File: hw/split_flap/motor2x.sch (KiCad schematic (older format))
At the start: 4 parts, among them J10 Conn_01x05, J9 Conn_01x05, U3 PCF8574, U4 ULN2803A

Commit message: hw: Supercharge PCB !
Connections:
- net L2: now reaches U4.6 (I6)
- net L2: now also U3.5 (P1); no longer U3.10 (P5)
- net L3: now reaches U4.7 (I7)
- net L3: now also U3.6 (P2); no longer U3.11 (P6)
- net L4: now reaches U4.8 (I8)
- net L4: now also U3.7 (P3); no longer U3.12 (P7)
- net L1: now reaches U3.4 (P0)
- net L1: now also U4.5 (I5); no longer U4.4 (I4)
- net L7: now reaches U4.3 (I3)
- net L7: now also U3.11 (P6); no longer U3.5 (P1)
- net L6: now reaches U4.2 (I2)
- net L6: now also U3.10 (P5); no longer U3.6 (P2)
- net L5: now reaches U4.1 (I1)
- net L5: now also U3.9 (P4); no longer U3.7 (P3)
- new net L8: U3.12 (P7), U4.4 (I4)
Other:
- moved on the sheet: J21, J22, U13, U14

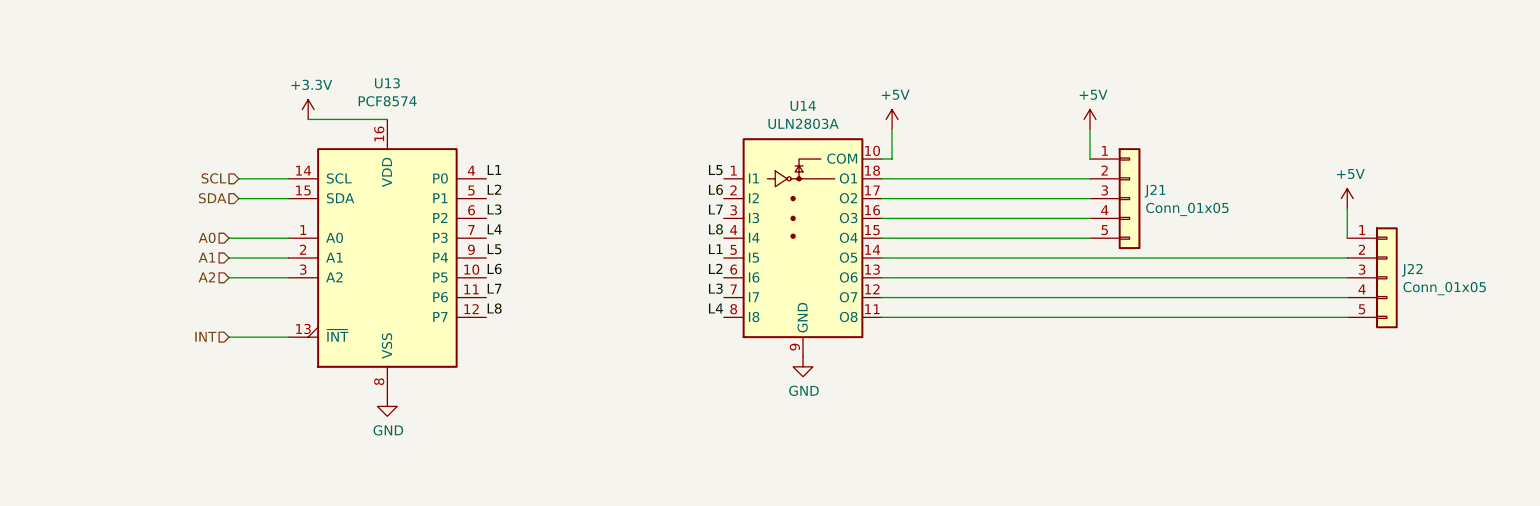
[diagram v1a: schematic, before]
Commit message: Reroute full PCB
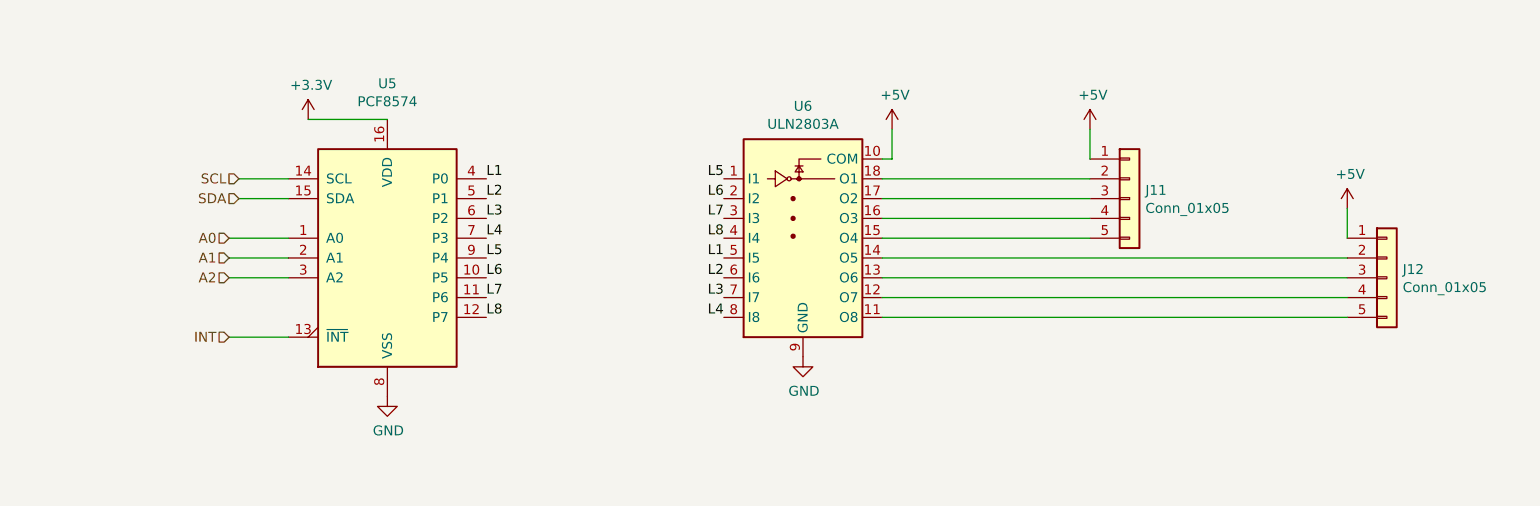
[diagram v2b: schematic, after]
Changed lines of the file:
@@
 AR Path="/5DEBFEF8/5E0DED8E" Ref="#PWR0150"  Part="1"
 AR Path="/5DED9C19/5E0DED8E" Ref="#PWR0156"  Part="1"
-F 0 "#PWR0156" H 9350 3000 50  0001 C CNN
+F 0 "#PWR0128" H 9350 3000 50  0001 C CNN
 F 1 "+5V" H 9365 3323 50  0000 C CNN
 F 2 "" H 9350 3150 50  0001 C CNN
@@
 AR Path="/5DEBFEF8/5E0DED94" Ref="J20"  Part="1"
 AR Path="/5DED9C19/5E0DED94" Ref="J22"  Part="1"
-F 0 "J22" H 9630 3542 50  0000 L CNN
+F 0 "J12" H 9630 3542 50  0000 L CNN
 F 1 "Conn_01x05" H 9630 3451 50  0000 L CNN
 F 2 "Connector_JST:JST_XH_B5B-XH-A_1x05_P2.50mm_Vertical" H 9550 3500 50  0001 C CNN
@@
 AR Path="/5DEBFEF8/5E0DED9D" Ref="#PWR0151"  Part="1"
 AR Path="/5DED9C19/5E0DED9D" Ref="#PWR0157"  Part="1"
-F 0 "#PWR0157" H 8050 2600 50  0001 C CNN
+F 0 "#PWR0129" H 8050 2600 50  0001 C CNN
 F 1 "+5V" H 8065 2923 50  0000 C CNN
 F 2 "" H 8050 2750 50  0001 C CNN
@@
 AR Path="/5DEBFEF8/5E0DEDA9" Ref="#PWR0152"  Part="1"
 AR Path="/5DED9C19/5E0DEDA9" Ref="#PWR0158"  Part="1"
-F 0 "#PWR0158" H 7050 2600 50  0001 C CNN
+F 0 "#PWR0131" H 7050 2600 50  0001 C CNN
 F 1 "+5V" H 7065 2923 50  0000 C CNN
 F 2 "" H 7050 2750 50  0001 C CNN
@@
 AR Path="/5DEBFEF8/5E0DEDAF" Ref="#PWR0153"  Part="1"
 AR Path="/5DED9C19/5E0DEDAF" Ref="#PWR0159"  Part="1"
-F 0 "#PWR0159" H 4500 3850 50  0001 C CNN
+F 0 "#PWR0132" H 4500 3850 50  0001 C CNN
 F 1 "GND" H 4505 3927 50  0000 C CNN
 F 2 "" H 4500 4100 50  0001 C CNN
@@
 AR Path="/5DEBFEF8/5E0DEDB5" Ref="#PWR0154"  Part="1"
 AR Path="/5DED9C19/5E0DEDB5" Ref="#PWR0160"  Part="1"
-F 0 "#PWR0160" H 6600 3650 50  0001 C CNN
+F 0 "#PWR0133" H 6600 3650 50  0001 C CNN
 F 1 "GND" H 6605 3727 50  0000 C CNN
 F 2 "" H 6600 3900 50  0001 C CNN
@@
 AR Path="/5DEBFEF8/5E0DEDBB" Ref="J18"  Part="1"
 AR Path="/5DED9C19/5E0DEDBB" Ref="J21"  Part="1"
-F 0 "J21" H 8330 3142 50  0000 L CNN
+F 0 "J11" H 8330 3142 50  0000 L CNN
 F 1 "Conn_01x05" H 8330 3051 50  0000 L CNN
 F 2 "Connector_JST:JST_XH_B5B-XH-A_1x05_P2.50mm_Vertical" H 8250 3100 50  0001 C CNN
@@
 AR Path="/5DEBFEF8/5E0DEDC5" Ref="U11"  Part="1"
 AR Path="/5DED9C19/5E0DEDC5" Ref="U13"  Part="1"
-F 0 "U13" H 4500 4281 50  0000 C CNN
+F 0 "U5" H 4500 4281 50  0000 C CNN
 F 1 "PCF8574" H 4500 4190 50  0000 C CNN
 F 2 "Package_SO:SOIC-16W_7.5x10.3mm_P1.27mm" H 4500 3400 50  0001 C CNN
@@
 AR Path="/5DEBFEF8/5E0DEDCB" Ref="U12"  Part="1"
 AR Path="/5DED9C19/5E0DEDCB" Ref="U14"  Part="1"
-F 0 "U14" H 6600 3767 50  0000 C CNN
+F 0 "U6" H 6600 3767 50  0000 C CNN
 F 1 "ULN2803A" H 6600 3676 50  0000 C CNN
 F 2 "Package_SO:SOP-18_7x12.5mm_P1.27mm" H 6650 2550 50  0001 L CNN
@@
 AR Path="/5DEBFEF8/5E2206F1" Ref="#PWR0155"  Part="1"
 AR Path="/5DED9C19/5E2206F1" Ref="#PWR0161"  Part="1"
-F 0 "#PWR0161" H 4100 2550 50  0001 C CNN
+F 0 "#PWR06" H 4100 2550 50  0001 C CNN
 F 1 "+3.3V" H 4115 2873 50  0000 C CNN
 F 2 "" H 4100 2700 50  0001 C CNN

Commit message: hw: Route pcb completely
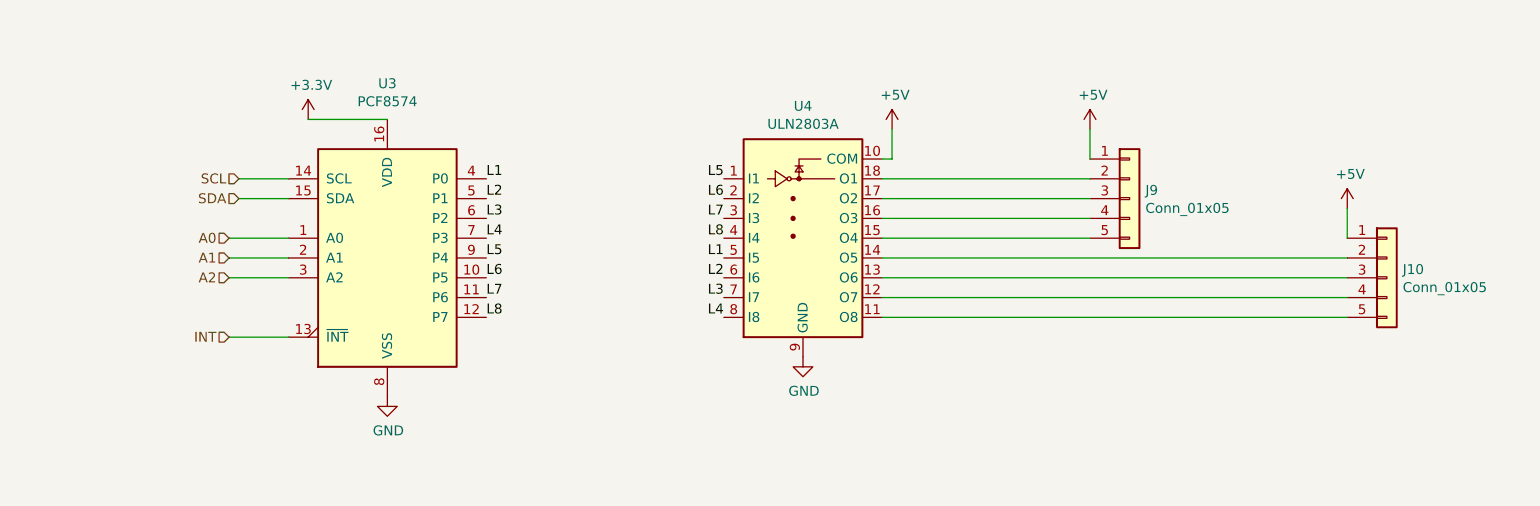
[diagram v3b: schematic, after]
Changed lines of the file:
@@
 $Descr A4 11693 8268
 encoding utf-8
-Sheet 3 7
+Sheet 2 7
 Title ""
 Date ""
@@
 AR Path="/5DEBFEF8/5E0DED8E" Ref="#PWR0150"  Part="1"
 AR Path="/5DED9C19/5E0DED8E" Ref="#PWR0156"  Part="1"
-F 0 "#PWR0128" H 9350 3000 50  0001 C CNN
+F 0 "#PWR0156" H 9350 3000 50  0001 C CNN
 F 1 "+5V" H 9365 3323 50  0000 C CNN
 F 2 "" H 9350 3150 50  0001 C CNN
@@
 AR Path="/5DEBFEF8/5E0DED94" Ref="J20"  Part="1"
 AR Path="/5DED9C19/5E0DED94" Ref="J22"  Part="1"
-F 0 "J12" H 9630 3542 50  0000 L CNN
+F 0 "J10" H 9630 3542 50  0000 L CNN
 F 1 "Conn_01x05" H 9630 3451 50  0000 L CNN
 F 2 "Connector_JST:JST_XH_B5B-XH-A_1x05_P2.50mm_Vertical" H 9550 3500 50  0001 C CNN
@@
 AR Path="/5DEBFEF8/5E0DED9D" Ref="#PWR0151"  Part="1"
 AR Path="/5DED9C19/5E0DED9D" Ref="#PWR0157"  Part="1"
-F 0 "#PWR0129" H 8050 2600 50  0001 C CNN
+F 0 "#PWR0157" H 8050 2600 50  0001 C CNN
 F 1 "+5V" H 8065 2923 50  0000 C CNN
 F 2 "" H 8050 2750 50  0001 C CNN
@@
 AR Path="/5DEBFEF8/5E0DEDA9" Ref="#PWR0152"  Part="1"
 AR Path="/5DED9C19/5E0DEDA9" Ref="#PWR0158"  Part="1"
-F 0 "#PWR0131" H 7050 2600 50  0001 C CNN
+F 0 "#PWR0158" H 7050 2600 50  0001 C CNN
 F 1 "+5V" H 7065 2923 50  0000 C CNN
 F 2 "" H 7050 2750 50  0001 C CNN
@@
 AR Path="/5DEBFEF8/5E0DEDAF" Ref="#PWR0153"  Part="1"
 AR Path="/5DED9C19/5E0DEDAF" Ref="#PWR0159"  Part="1"
-F 0 "#PWR0132" H 4500 3850 50  0001 C CNN
+F 0 "#PWR0159" H 4500 3850 50  0001 C CNN
 F 1 "GND" H 4505 3927 50  0000 C CNN
 F 2 "" H 4500 4100 50  0001 C CNN
@@
 AR Path="/5DEBFEF8/5E0DEDB5" Ref="#PWR0154"  Part="1"
 AR Path="/5DED9C19/5E0DEDB5" Ref="#PWR0160"  Part="1"
-F 0 "#PWR0133" H 6600 3650 50  0001 C CNN
+F 0 "#PWR0160" H 6600 3650 50  0001 C CNN
 F 1 "GND" H 6605 3727 50  0000 C CNN
 F 2 "" H 6600 3900 50  0001 C CNN
@@
 AR Path="/5DEBFEF8/5E0DEDBB" Ref="J18"  Part="1"
 AR Path="/5DED9C19/5E0DEDBB" Ref="J21"  Part="1"
-F 0 "J11" H 8330 3142 50  0000 L CNN
+F 0 "J9" H 8330 3142 50  0000 L CNN
 F 1 "Conn_01x05" H 8330 3051 50  0000 L CNN
 F 2 "Connector_JST:JST_XH_B5B-XH-A_1x05_P2.50mm_Vertical" H 8250 3100 50  0001 C CNN
@@
 AR Path="/5DEBFEF8/5E0DEDC5" Ref="U11"  Part="1"
 AR Path="/5DED9C19/5E0DEDC5" Ref="U13"  Part="1"
-F 0 "U5" H 4500 4281 50  0000 C CNN
+F 0 "U3" H 4500 4281 50  0000 C CNN
 F 1 "PCF8574" H 4500 4190 50  0000 C CNN
 F 2 "Package_SO:SOIC-16W_7.5x10.3mm_P1.27mm" H 4500 3400 50  0001 C CNN
@@
 AR Path="/5DEBFEF8/5E0DEDCB" Ref="U12"  Part="1"
 AR Path="/5DED9C19/5E0DEDCB" Ref="U14"  Part="1"
-F 0 "U6" H 6600 3767 50  0000 C CNN
+F 0 "U4" H 6600 3767 50  0000 C CNN
 F 1 "ULN2803A" H 6600 3676 50  0000 C CNN
 F 2 "Package_SO:SOP-18_7x12.5mm_P1.27mm" H 6650 2550 50  0001 L CNN
@@
 AR Path="/5DEBFEF8/5E2206F1" Ref="#PWR0155"  Part="1"
 AR Path="/5DED9C19/5E2206F1" Ref="#PWR0161"  Part="1"
-F 0 "#PWR06" H 4100 2550 50  0001 C CNN
+F 0 "#PWR0161" H 4100 2550 50  0001 C CNN
 F 1 "+3.3V" H 4115 2873 50  0000 C CNN
 F 2 "" H 4100 2700 50  0001 C CNN

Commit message: Update schematic with 74HC595
Remove PCF for output and use shift register
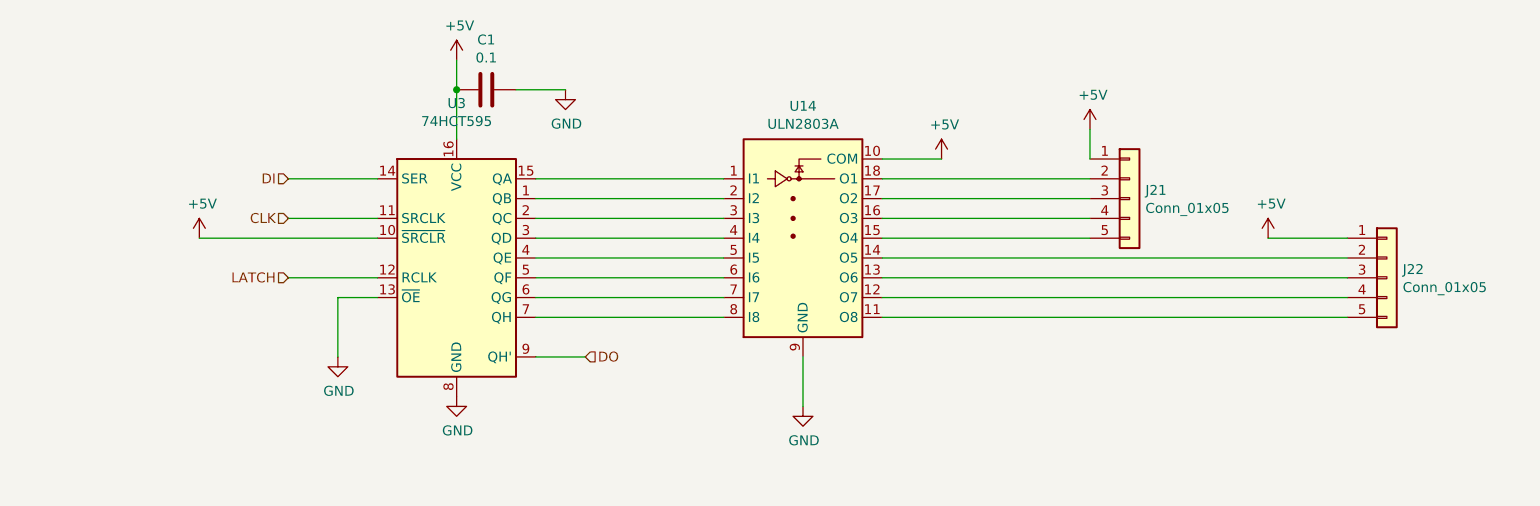
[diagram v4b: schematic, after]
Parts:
- removed U3: PCF8574, Package_SO:SOIC-16W_7.5x10.3mm_P1.27mm, symbol Interface_Expansion:PCF8574
- added C1: 0.1, symbol Device:C
- added U3: 74HCT595, symbol 74xx:74HCT595
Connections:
- net +5V: now also C1.1, U3.10 (~SRCLR), U3.16 (VCC)
- net GND: now also C1.2, U3.13 (~OE), U3.8 (GND)
- net L1: no longer names the net of U4.5 (I5)
- net L1: now also U3.4 (QE)
- net L2: no longer names the net of U4.6 (I6)
- net L2: now also U3.5 (QF)
- net L3: no longer names the net of U4.7 (I7)
- net L3: now also U3.6 (QG)
- net L4: no longer names the net of U4.8 (I8)
- net L4: now also U3.7 (QH)
- net L5: no longer names the net of U4.1 (I1)
- net L5: now also U3.15 (QA)
- net L6: no longer names the net of U4.2 (I2)
- net L6: now also U3.1 (QB)
- net L7: no longer names the net of U4.3 (I3)
- net L7: now also U3.2 (QC)
- net L8: no longer names the net of U4.4 (I4)
- net L8: now also U3.3 (QD)
- new net CLK: U3.11 (SRCLK)
- new net DI: U3.14 (SER)
- new net DO: U3.9 (QH')
- new net LATCH: U3.12 (RCLK)

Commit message: Rework PCB
Start routing all expanders
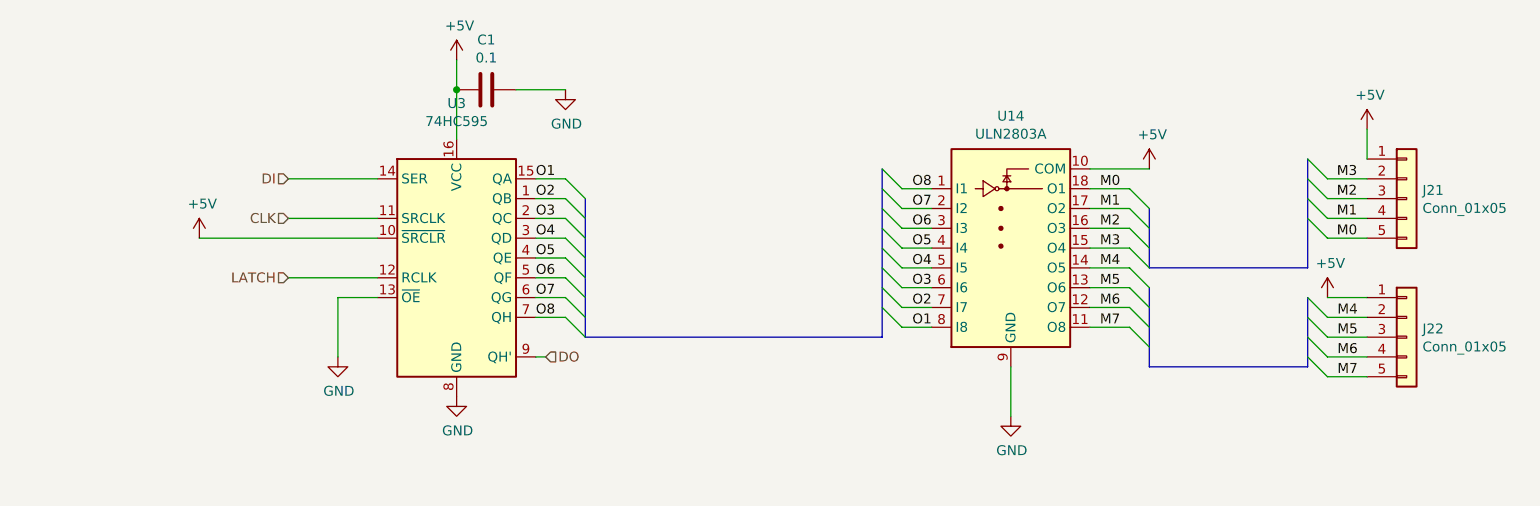
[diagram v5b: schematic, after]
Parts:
- removed U3: 74HCT595, symbol 74xx:74HCT595
- added U9: 74HC595, Package_SO:SOP-16_4.55x10.3mm_P1.27mm, symbol 74xx:74HC595
- C1: footprint (none) -> Capacitor_THT:C_Disc_D4.3mm_W1.9mm_P5.00mm
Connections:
- net +5V: now also U9.10 (~SRCLR), U9.16 (VCC)
- net CLK: now also U9.11 (SRCLK)
- net DI: now also U9.14 (SER)
- net DO: now also U9.9 (QH')
- net GND: now also U9.13 (~OE), U9.8 (GND)
- net LATCH: now also U9.12 (RCLK)
- net O7: now reaches U4.2 (I2)
- net O7: now also U9.6 (QG)
- net O8: now reaches U4.1 (I1)
- net O8: now also U9.7 (QH)
- net O6: now reaches U4.3 (I3)
- net O6: now also U9.5 (QF)
- net O5: now reaches U4.4 (I4)
- net O5: now also U9.4 (QE)
- net O4: now reaches U4.5 (I5)
- net O4: now also U9.3 (QD)
- net O3: now reaches U4.6 (I6)
- net O3: now also U9.2 (QC)
- net O2: now reaches U4.7 (I7)
- net O2: now also U9.1 (QB)
- net O1: now reaches U4.8 (I8)
- net O1: now also U9.15 (QA)
- net M4: now reaches J10.2 (Pin_2), U4.14 (O5)
- net M5: now reaches J10.3 (Pin_3), U4.13 (O6)
- net M6: now reaches J10.4 (Pin_4), U4.12 (O7)
- net M7: now reaches J10.5 (Pin_5), U4.11 (O8)
- net M0: now reaches U4.18 (O1)
- net M0: now also J9.5 (Pin_5); no longer J9.2 (Pin_2)
- net M1: now reaches U4.17 (O2)
- net M1: now also J9.4 (Pin_4); no longer J9.3 (Pin_3)
- net M2: now reaches U4.16 (O3)
- net M2: now also J9.3 (Pin_3); no longer J9.4 (Pin_4)
- net M3: now reaches U4.15 (O4)
- net M3: now also J9.2 (Pin_2); no longer J9.5 (Pin_5)
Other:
- moved on the sheet: J21, J22, U14

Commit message: Route new PCB completely.
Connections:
- net +5V: now also J10.5 (Pin_5), J9.5 (Pin_5); no longer J10.1 (Pin_1), J9.1 (Pin_1)
- net M0: now also J9.1 (Pin_1); no longer J9.5 (Pin_5)
- net M1: now also J9.2 (Pin_2); no longer J9.4 (Pin_4)
- net M3: now also J9.4 (Pin_4); no longer J9.2 (Pin_2)
- net M4: now also J10.4 (Pin_4); no longer J10.2 (Pin_2)
- net M6: now also J10.2 (Pin_2); no longer J10.4 (Pin_4)
- net M7: now also J10.1 (Pin_1); no longer J10.5 (Pin_5)
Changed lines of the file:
@@
 $Descr A4 11693 8268
 encoding utf-8
-Sheet 2 6
+Sheet 5 6
 Title ""
 Date ""
@@
 AR Path="/5E0964A4/5E0DEDAF" Ref="#PWR033"  Part="1"
 AR Path="/5E0B21A0/5E0DEDAF" Ref="#PWR051"  Part="1"
-F 0 "#PWR051" H 4850 3850 50  0001 C CNN
+F 0 "#PWR042" H 4850 3850 50  0001 C CNN
 F 1 "GND" H 4855 3927 50  0000 C CNN
 F 2 "" H 4850 4100 50  0001 C CNN
@@
 AR Path="/5E0964A4/5DF98B62" Ref="#PWR032"  Part="1"
 AR Path="/5E0B21A0/5DF98B62" Ref="#PWR050"  Part="1"
-F 0 "#PWR050" H 4850 2250 50  0001 C CNN
+F 0 "#PWR041" H 4850 2250 50  0001 C CNN
 F 1 "+5V" H 4865 2573 50  0000 C CNN
 F 2 "" H 4850 2400 50  0001 C CNN
@@
 AR Path="/5E0964A4/5DF9B643" Ref="#PWR031"  Part="1"
 AR Path="/5E0B21A0/5DF9B643" Ref="#PWR049"  Part="1"
-F 0 "#PWR049" H 4250 3650 50  0001 C CNN
+F 0 "#PWR040" H 4250 3650 50  0001 C CNN
 F 1 "GND" H 4255 3727 50  0000 C CNN
 F 2 "" H 4250 3900 50  0001 C CNN
@@
 AR Path="/5E0964A4/5DF9D02C" Ref="#PWR030"  Part="1"
 AR Path="/5E0B21A0/5DF9D02C" Ref="#PWR048"  Part="1"
-F 0 "#PWR048" H 3550 3150 50  0001 C CNN
+F 0 "#PWR039" H 3550 3150 50  0001 C CNN
 F 1 "+5V" H 3565 3473 50  0000 C CNN
 F 2 "" H 3550 3300 50  0001 C CNN
@@
 AR Path="/5E092C79/5E0E710C" Ref="C3"  Part="1"
 AR Path="/5E0B21A0/5E0E710C" Ref="C4"  Part="1"
-F 0 "C1" V 5252 2550 50  0000 C CNN
+F 0 "C3" V 5252 2550 50  0000 C CNN
 F 1 "0.1" V 5161 2550 50  0000 C CNN
 F 2 "Capacitor_THT:C_Disc_D4.3mm_W1.9mm_P5.00mm" H 5038 2400 50  0001 C CNN
@@
 AR Path="/5E0964A4/5E0E7881" Ref="#PWR034"  Part="1"
 AR Path="/5E0B21A0/5E0E7881" Ref="#PWR052"  Part="1"
-F 0 "#PWR052" H 5400 2300 50  0001 C CNN
+F 0 "#PWR043" H 5400 2300 50  0001 C CNN
 F 1 "GND" H 5405 2377 50  0000 C CNN
 F 2 "" H 5400 2550 50  0001 C CNN
@@
 AR Path="/5E0964A4/5DF4397F" Ref="U5"  Part="1"
 AR Path="/5E092C79/5DF4397F" Ref="U7"  Part="1"
-F 0 "U3" H 4850 4181 50  0000 C CNN
+F 0 "U7" H 4850 4181 50  0000 C CNN
 F 1 "74HC595" H 4850 4090 50  0000 C CNN
 F 2 "Package_SO:SOP-16_4.55x10.3mm_P1.27mm" H 4850 3400 50  0001 C CNN
@@
 AR Path="/5E0964A4/5E0DED8E" Ref="#PWR038"  Part="1"
 AR Path="/5E0B21A0/5E0DED8E" Ref="#PWR056"  Part="1"
-F 0 "#PWR056" H 9250 3450 50  0001 C CNN
+F 0 "#PWR047" H 9250 3450 50  0001 C CNN
 F 1 "+5V" H 9265 3773 50  0000 C CNN
 F 2 "" H 9250 3600 50  0001 C CNN
@@
 AR Path="/5E0964A4/5E0DED94" Ref="J10"  Part="1"
 AR Path="/5E0B21A0/5E0DED94" Ref="J14"  Part="1"
-F 0 "J22" H 9730 3842 50  0000 L CNN
+F 0 "J12" H 9730 3842 50  0000 L CNN
 F 1 "Conn_01x05" H 9730 3751 50  0000 L CNN
 F 2 "Connector_JST:JST_XH_B5B-XH-A_1x05_P2.50mm_Vertical" H 9650 3800 50  0001 C CNN
 F 3 "~" H 9650 3800 50  0001 C CNN
 	1    9650 3800
-	1    0    0    -1
+	1    0    0    1
 $EndComp
 Wire Wire Line
@@
 AR Path="/5E0964A4/5E0DED9D" Ref="#PWR037"  Part="1"
 AR Path="/5E0B21A0/5E0DED9D" Ref="#PWR055"  Part="1"
-F 0 "#PWR055" H 9450 2600 50  0001 C CNN
+F 0 "#PWR046" H 9450 2600 50  0001 C CNN
 F 1 "+5V" H 9465 2923 50  0000 C CNN
 F 2 "" H 9450 2750 50  0001 C CNN
@@
 AR Path="/5E0964A4/5E0DEDA9" Ref="#PWR036"  Part="1"
 AR Path="/5E0B21A0/5E0DEDA9" Ref="#PWR054"  Part="1"
-F 0 "#PWR054" H 8350 2800 50  0001 C CNN
+F 0 "#PWR045" H 8350 2800 50  0001 C CNN
 F 1 "+5V" H 8365 3123 50  0000 C CNN
 F 2 "" H 8350 2950 50  0001 C CNN
@@
 AR Path="/5E0964A4/5E0DEDB5" Ref="#PWR035"  Part="1"
 AR Path="/5E0B21A0/5E0DEDB5" Ref="#PWR053"  Part="1"
-F 0 "#PWR053" H 7650 3950 50  0001 C CNN
+F 0 "#PWR044" H 7650 3950 50  0001 C CNN
 F 1 "GND" H 7655 4027 50  0000 C CNN
 F 2 "" H 7650 4200 50  0001 C CNN
@@
 AR Path="/5E0964A4/5E0DEDBB" Ref="J9"  Part="1"
 AR Path="/5E0B21A0/5E0DEDBB" Ref="J13"  Part="1"
-F 0 "J21" H 9730 3142 50  0000 L CNN
+F 0 "J11" H 9730 3142 50  0000 L CNN
 F 1 "Conn_01x05" H 9730 3051 50  0000 L CNN
 F 2 "Connector_JST:JST_XH_B5B-XH-A_1x05_P2.50mm_Vertical" H 9650 3100 50  0001 C CNN
 F 3 "~" H 9650 3100 50  0001 C CNN
 	1    9650 3100
-	1    0    0    -1
+	1    0    0    1
 $EndComp
 $Comp
@@
 AR Path="/5E0964A4/5E0DEDCB" Ref="U6"  Part="1"
 AR Path="/5E0B21A0/5E0DEDCB" Ref="U10"  Part="1"
-F 0 "U14" H 7650 3817 50  0000 C CNN
+F 0 "U8" H 7650 3817 50  0000 C CNN
 F 1 "ULN2803A" H 7650 3726 50  0000 C CNN
 F 2 "Package_SO:SOP-18_7x12.5mm_P1.27mm" H 7700 2600 50  0001 L CNN
